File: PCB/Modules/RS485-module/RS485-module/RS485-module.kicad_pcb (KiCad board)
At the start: 2 copper layers, 8 parts, among them U1 THVD1400D

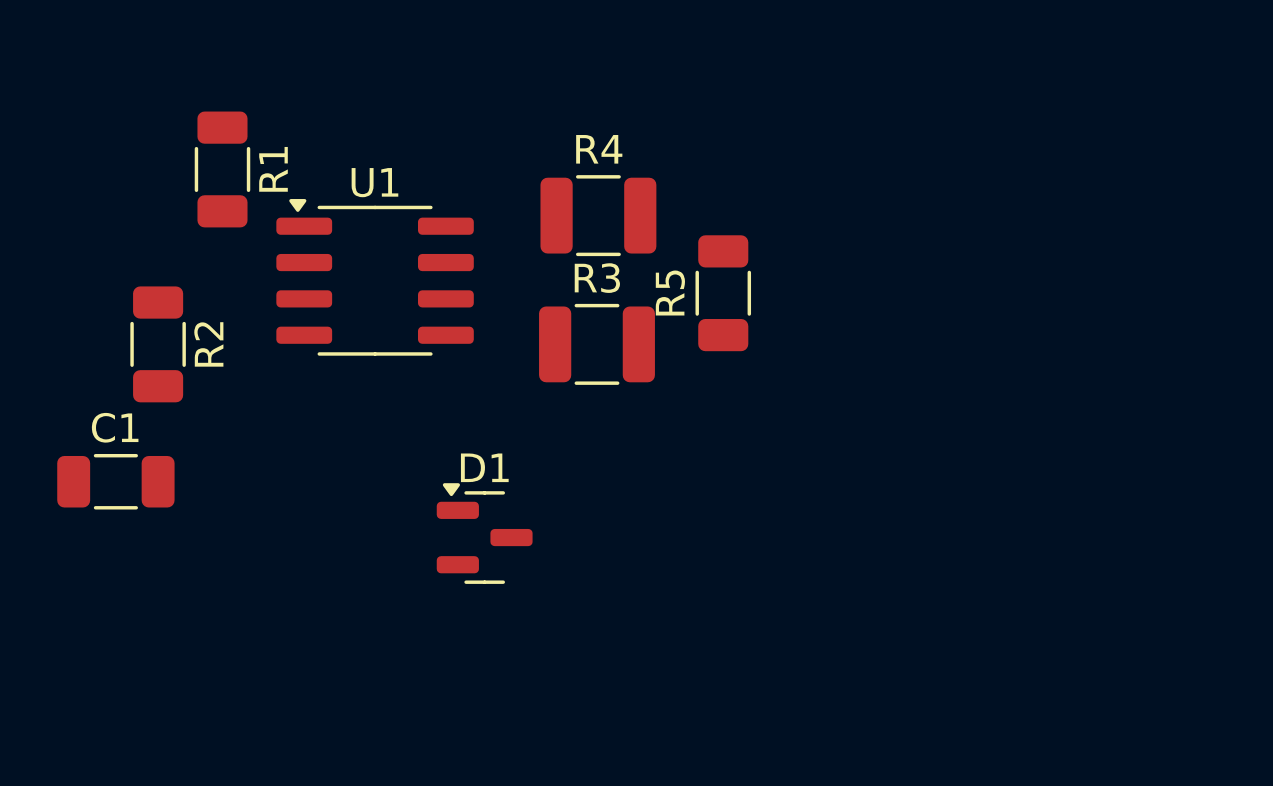
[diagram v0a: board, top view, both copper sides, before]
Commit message: Added switch modules and RS485 module
Signed-off-by: Simonca Raul <simonca.raul@gmail.com>
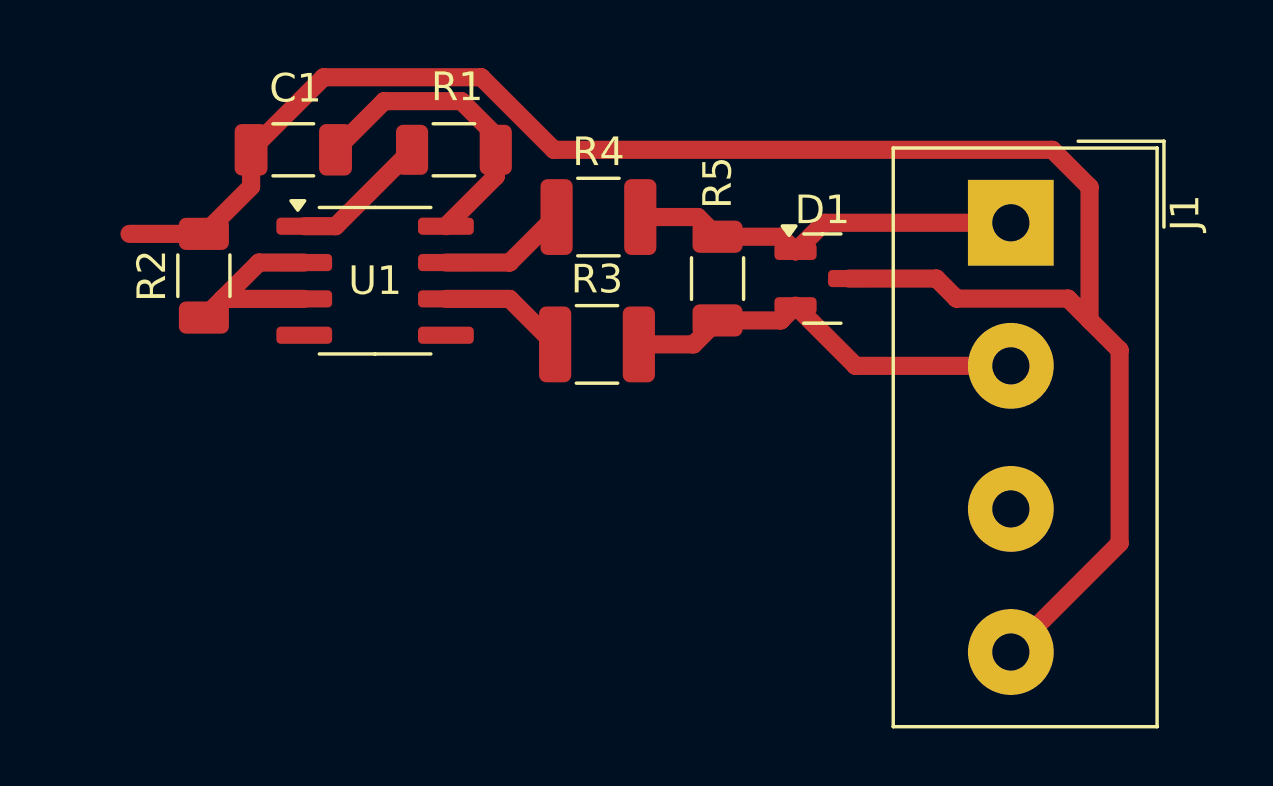
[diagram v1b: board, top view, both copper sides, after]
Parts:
- added J1: Screw_Terminal_01x04, TerminalBlock_Altech:Altech_AK100_1x04_P5.00mm, F.Cu at (177.1, 95.8)
- moved D1 14.9 mm to (170.5, 97.8)
- moved C1 13.2 mm to (152.0, 93.3), turned to 180 degrees
- moved R1 8.12 mm to (157.6, 93.3), turned to 180 degrees
- moved R2 2.88 mm to (148.8, 97.7), turned to 90 degrees
- moved R5 0.55 mm to (166.8, 97.8)
- moved R4 0.05 mm to (162.6, 95.7)
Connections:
- net Net-(U1-A) renamed /Bout
- net Net-(U1-B) renamed /Aout
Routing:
- net GND: track 0.00 -> 65.4 mm
- net /A: track 0.00 -> 14.4 mm
- net /B: track 0.00 -> 13.9 mm
- net +5V: track 0.00 -> 10.7 mm
- net /XDIR: track 0.00 -> 7.16 mm
- net /RxD: track 0.00 -> 4.87 mm
- net /Aout: track 0.00 -> 4.55 mm
- net /Bout: track 0.00 -> 4.48 mm
